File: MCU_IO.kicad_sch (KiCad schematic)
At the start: 31 parts, among them Q1 IRLML2803, SW1 SW_Omron_B3FS, SW2 SW_Omron_B3FS, U1 W25Q64JVSS, U2 RP2040, U3 MAX706RESA+, Y1 12MHz

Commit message: temp
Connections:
- net MCU_RX_Jetson is gone; now on net LoRa_CSn: U2.28 (GPIO17)
- net SD_CLK is gone; now on net LoRa_TX_EN: U2.34 (GPIO22)
- net SD_MISO is gone; now on net LoRa_RX_EN: U2.31 (GPIO20)
- net SD_MOSI is gone; now on net LoRa_BUSY: U2.35 (GPIO23)
- net 3V3_RST: no longer U2.9 (GPIO7)
- net Battery_ALERT: no longer U2.37 (GPIO25)
- net GPS_EN: no longer U2.8 (GPIO6)
- net I2C0_SCL: no longer U2.3 (GPIO1)
- net I2C0_SDA: no longer U2.2 (GPIO0)
- net I2C1_SCL: no longer U2.5 (GPIO3)
- net I2C1_SDA: no longer U2.4 (GPIO2)
- net IMU_INTn: no longer U2.29 (GPIO18)
- net IMU_RSTn: no longer U2.30 (GPIO19)
- net Jetson_EN: no longer U2.36 (GPIO24)
- net LoRa_BUSY: no longer U2.17 (GPIO14)
- net LoRa_CSn: no longer U2.12 (GPIO9)
- net LoRa_DIO1: now also U2.37 (GPIO25); no longer U2.38 (GPIO26_ADC0)
- net LoRa_DIO2: now also U2.36 (GPIO24); no longer U2.39 (GPIO27_ADC1)
- net LoRa_EN: no longer U2.15 (GPIO12)
- net LoRa_RSTn: now also U2.32 (GPIO21); no longer U2.16 (GPIO13)
- net LoRa_RX_EN: no longer U2.40 (GPIO28_ADC2)
- net LoRa_TX_EN: no longer U2.41 (GPIO29_ADC3)
- net SD_CSn: now also U2.38 (GPIO26_ADC0); no longer U2.32 (GPIO21)
- net WDT_WDI: no longer U2.18 (GPIO15)
- net LoRa_CLK: no longer names the net of U2.13 (GPIO10)
- net LoRa_MISO: no longer names the net of U2.11 (GPIO8)
- net LoRa_MOSI: no longer names the net of U2.14 (GPIO11)
- net MCU_RX_GPS: no longer names the net of U2.7 (GPIO5)
- net MCU_TX_GPS: no longer names the net of U2.6 (GPIO4)
- net MCU_TX_Jetson renamed SPI0_MISO
- new net SPI0_CLK: U2.29 (GPIO18)
- new net SPI0_MOSI: U2.30 (GPIO19)

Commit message: v1 done
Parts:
- removed C10: 2u2, Capacitor_SMD:C_0603_1608Metric, symbol Device:C_Small
- added C25: 2u2, Capacitor_SMD:C_0603_1608Metric, symbol Device:C_Small
- SW1, SW2: footprint Button_Switch_SMD:SW_SPST_Omron_B3FS-100xP -> Button_Switch_SMD:SW_SPST_Omron_B3FS-105xP
- U3: symbol MainBoard:MAX706RESA+ -> Argus-IC:MAX706RESA+
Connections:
- net +1V1: now also C25.1
- net 3V3_RST: now also U2.9 (GPIO7)
- net GND: now also C25.2
- net GPS_EN: now also U2.39 (GPIO27_ADC1)
- net I2C0_SCL: now also U2.3 (GPIO1)
- net I2C0_SDA: now also U2.2 (GPIO0)
- net I2C1_SCL: now also U2.5 (GPIO3)
- net I2C1_SDA: now also U2.4 (GPIO2)
- net IMU_INTn: now also U2.41 (GPIO29_ADC3)
- net Jetson_CSn: now also U2.12 (GPIO9)
- net LoRa_EN: now also U2.40 (GPIO28_ADC2)
- net SPI1_CLK: now also U2.13 (GPIO10)
- net SPI1_MISO: now also U2.11 (GPIO8)
- net SPI1_MOSI: now also U2.14 (GPIO11)
- net UART0_RX: now also U2.16 (GPIO13)
- net UART0_TX: now also U2.15 (GPIO12)
- net UART1_RX: now also U2.7 (GPIO5)
- net UART1_TX: now also U2.6 (GPIO4)
- net WDT_WDI: now also U2.8 (GPIO6)
- net RS485_TX_EN: now reaches U2.17 (GPIO14)
- net RS485_RX_EN: now reaches U2.18 (GPIO15)

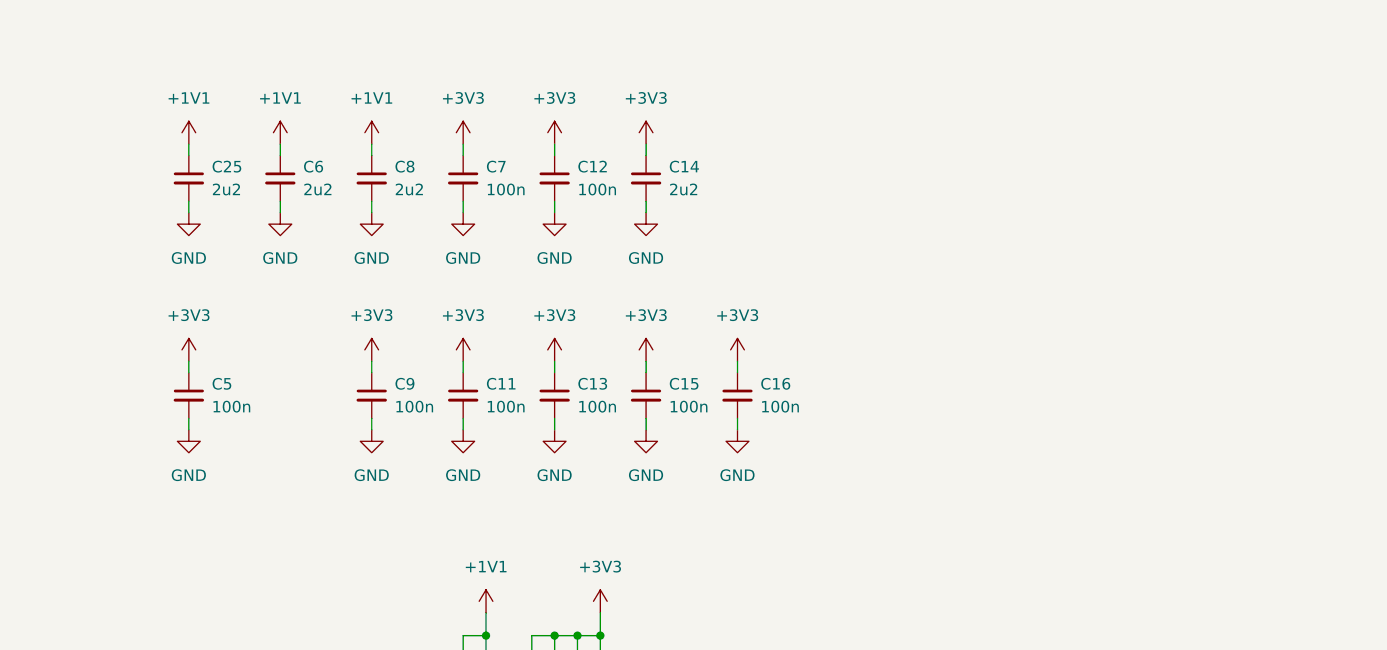
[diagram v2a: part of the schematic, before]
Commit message: Updated i2c device addresses and mcu caps
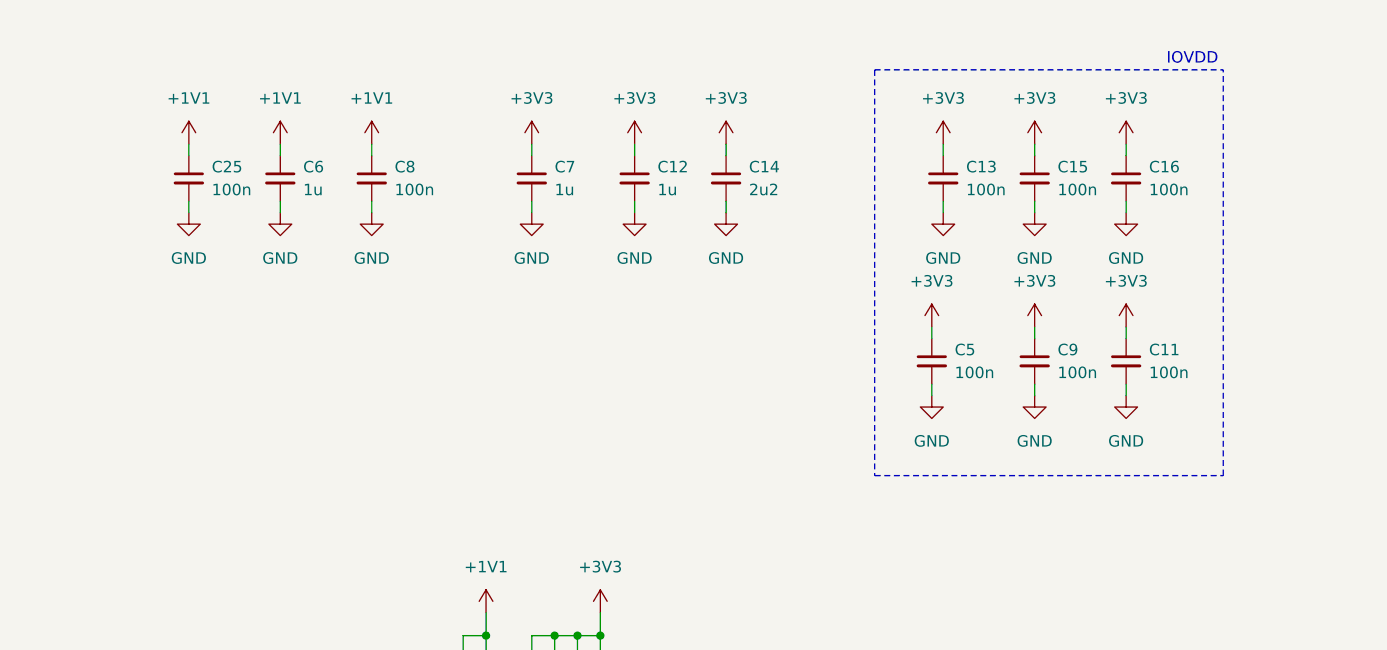
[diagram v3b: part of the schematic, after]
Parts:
- C12, C7: value 100n -> 1u
- C25, C8: value 2u2 -> 100n
- C6: value 2u2 -> 1u
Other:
- note added: "IOVDD"
- moved on the sheet: C11, C13, C15, C16, C5, C9

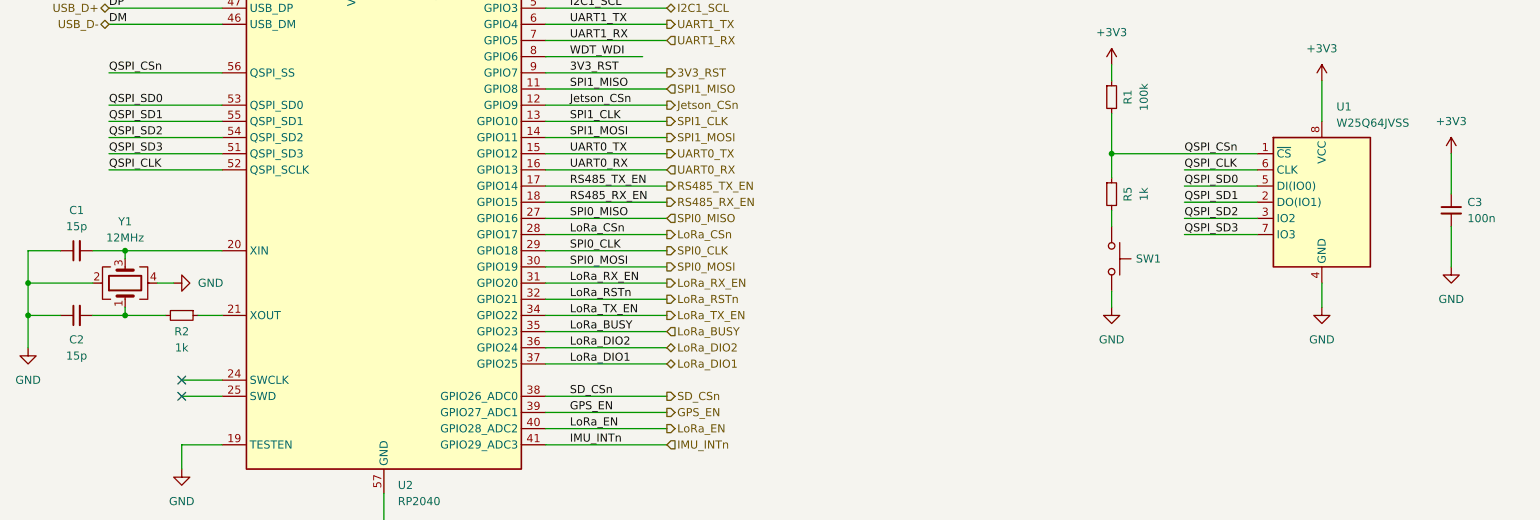
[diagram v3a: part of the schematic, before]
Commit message: Added extra connector
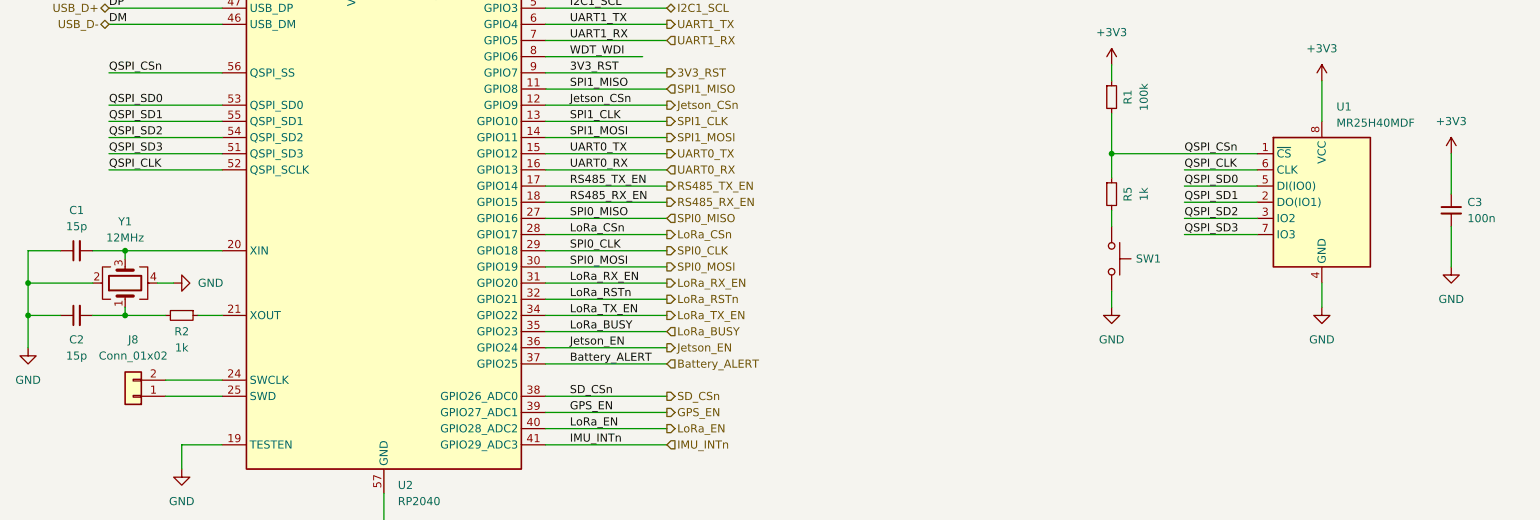
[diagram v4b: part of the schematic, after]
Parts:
- added J8: Conn_01x02, Connector_PinHeader_2.54mm:PinHeader_1x02_P2.54mm_Vertical, symbol Connector_Generic:Conn_01x02
- U1: value W25Q64JVSS -> MR25H40MDF; footprint Package_SO:SOIC-8_5.23x5.23mm_P1.27mm -> Package_DFN_QFN:DFN-8-1EP_6x5mm_P1.27mm_EP2x2mm
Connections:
- net at U2.24 (SWCLK): now also J8.2 (Pin_2)
- net at U2.25 (SWD): now also J8.1 (Pin_1)
- net LoRa_DIO1 renamed Battery_ALERT
- net LoRa_DIO2 renamed Jetson_EN
- no-connect marks 3 -> 1
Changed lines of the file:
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@@
 	)
 	(no_connect
-		(at 49.53 166.37)
-	)
-	(no_connect
 		(at 205.74 35.56)
 	)
-	(no_connect
-		(at 49.53 163.83)
-	)
 	(wire
 		(pts
@@
 	(wire
 		(pts
-			(xy 49.53 163.83) (xy 55.88 163.83)
-		)
-		(stroke
-			(width 0)
-			(type default)
-		)
-	)
-	(wire
-		(pts
 			(xy 195.58 149.86) (xy 195.58 152.4)
 		)
@@
 	(wire
 		(pts
+			(xy 46.99 163.83) (xy 55.88 163.83)
+		)
+		(stroke
+			(width 0)
+			(type default)
+		)
+	)
+	(wire
+		(pts
 			(xy 217.17 59.69) (xy 223.52 59.69)
 		)
@@
 	(wire
 		(pts
+			(xy 106.68 161.29) (xy 125.73 161.29)
+		)
+		(stroke
+			(width 0)
+			(type default)
+		)
+	)
+	(wire
+		(pts
 			(xy 106.68 120.65) (xy 125.73 120.65)
 		)
@@
 	(wire
 		(pts
-			(xy 106.68 158.75) (xy 125.73 158.75)
-		)
-		(stroke
-			(width 0)
-			(type default)
-		)
-	)
-	(wire
-		(pts
 			(xy 195.58 128.27) (xy 218.44 128.27)
 		)
@@
 	(wire
 		(pts
-			(xy 106.68 161.29) (xy 125.73 161.29)
-		)
-		(stroke
-			(width 0)
-			(type default)
-		)
-	)
-	(wire
-		(pts
 			(xy 223.52 72.39) (xy 219.71 72.39)
 		)
@@
 	(wire
 		(pts
+			(xy 46.99 166.37) (xy 55.88 166.37)
+		)
+		(stroke
+			(width 0)
+			(type default)
+		)
+	)
+	(wire
+		(pts
 			(xy 38.1 120.65) (xy 55.88 120.65)
 		)
@@
 	(wire
 		(pts
+			(xy 106.68 158.75) (xy 125.73 158.75)
+		)
+		(stroke
+			(width 0)
+			(type default)
+		)
+	)
+	(wire
+		(pts
 			(xy 193.04 38.1) (xy 193.04 40.64)
 		)
@@
 	(wire
 		(pts
-			(xy 49.53 166.37) (xy 55.88 166.37)
-		)
-		(stroke
-			(width 0)
-			(type default)
-		)
-	)
-	(wire
-		(pts
 			(xy 106.68 100.33) (xy 125.73 100.33)
 		)
@@
 		)
 	)
-	(label "LoRa_DIO2"
-		(at 110.49 158.75 0)
-		(fields_autoplaced yes)
-		(effects
-			(font
-				(size 1.27 1.27)
-			)
-			(justify left bottom)
-		)
-	)
 	(label "QSPI_SD3"
 		(at 38.1 128.27 0)
@@
 		)
 	)
+	(label "Battery_ALERT"
+		(at 110.49 161.29 0)
+		(fields_autoplaced yes)
+		(effects
+			(font
+				(size 1.27 1.27)
+			)
+			(justify left bottom)
+		)
+	)
 	(label "RESETn"
 		(at 194.31 72.39 0)
@@
 		)
 	)
-	(label "LoRa_DIO1"
-		(at 110.49 161.29 0)
+	(label "3V3_RST"
+		(at 110.49 115.57 0)
 		(fields_autoplaced yes)
 		(effects
@@
 		)
 	)
-	(label "3V3_RST"
-		(at 110.49 115.57 0)
+	(label "Jetson_EN"
+		(at 110.49 158.75 0)
 		(fields_autoplaced yes)
 		(effects
@@
 		)
 	)
-	(hierarchical_label "LoRa_DIO1"
-		(shape bidirectional)
-		(at 125.73 161.29 0)
-		(fields_autoplaced yes)
-		(effects
-			(font
-				(size 1.27 1.27)
-			)
-			(justify left)
-		)
-	)
 	(hierarchical_label "RS485_RX_EN"
 		(shape output)
@@
 		)
 	)
-	(hierarchical_label "I2C0_SDA"
-		(shape bidirectional)
-		(at 125.73 97.79 0)
+	(hierarchical_label "Battery_ALERT"
+		(shape input)
+		(at 125.73 161.29 0)
 		(fields_autoplaced yes)
 		(effects
@@
 		)
 	)
-	(hierarchical_label "LoRa_DIO2"
+	(hierarchical_label "I2C0_SDA"
 		(shape bidirectional)
-		(at 125.73 158.75 0)
+		(at 125.73 97.79 0)
 		(fields_autoplaced yes)
 		(effects
@@
 		)
 	)
+	(hierarchical_label "Jetson_EN"
+		(shape output)
+		(at 125.73 158.75 0)
+		(fields_autoplaced yes)
+		(effects
+			(font
+				(size 1.27 1.27)
+			)
+			(justify left)
+		)
+	)
 	(hierarchical_label "SPI1_MISO"
 		(shape input)
@@
 	)
 	(symbol
+		(lib_id "Connector_Generic:Conn_01x02")
+		(at 41.91 166.37 180)
+		(unit 1)
+		(exclude_from_sim no)
+		(in_bom yes)
+		(on_board yes)
+		(dnp no)
+		(fields_autoplaced yes)
+		(property "Reference" "J8"
+			(at 41.91 157.48 0)
+			(effects
+				(font
+					(size 1.27 1.27)
+				)
+			)
+		)
+		(property "Value" "Conn_01x02"
+			(at 41.91 160.02 0)
+			(effects
+				(font
+					(size 1.27 1.27)
+				)
+			)
+		)
+		(property "Footprint" "Connector_PinHeader_2.54mm:PinHeader_1x02_P2.54mm_Vertical"
+			(at 41.91 166.37 0)
+			(effects
+				(font
+					(size 1.27 1.27)
+				)
+				(hide yes)
+			)
+		)
+		(property "Datasheet" "~"
+			(at 41.91 166.37 0)
+			(effects
+				(font
+					(size 1.27 1.27)
+				)
+				(hide yes)
+			)
+		)
+		(property "Description" "Generic connector, single row, 01x02, script generated (kicad-library-utils/schlib/autogen/connector/)"
+			(at 41.91 166.37 0)
+			(effects
+				(font
+					(size 1.27 1.27)
+				)
+				(hide yes)
+			)
+		)
+		(pin "2"
+		)
+		(pin "1"
+		)
+		(instances
+			(project ""
+				(path "/4c932743-8c6f-426e-9c1f-5a3f2b32c70d/21e71e76-dfb6-4af2-84cc-797c0fdddabe"
+					(reference "J8")
+					(unit 1)
+				)
+			)
+		)
+	)
+	(symbol
 		(lib_id "Device:R_Small")
 		(at 195.58 134.62 0)
@@
 			)
 		)
-		(property "Value" "W25Q64JVSS"
+		(property "Value" "MR25H40MDF"
 			(at 230.886 123.444 0)
 			(effects
@@
 			)
 		)
-		(property "Footprint" "Package_SO:SOIC-8_5.23x5.23mm_P1.27mm"
+		(property "Footprint" "Package_DFN_QFN:DFN-8-1EP_6x5mm_P1.27mm_EP2x2mm"
 			(at 228.6 135.89 0)
 			(effects

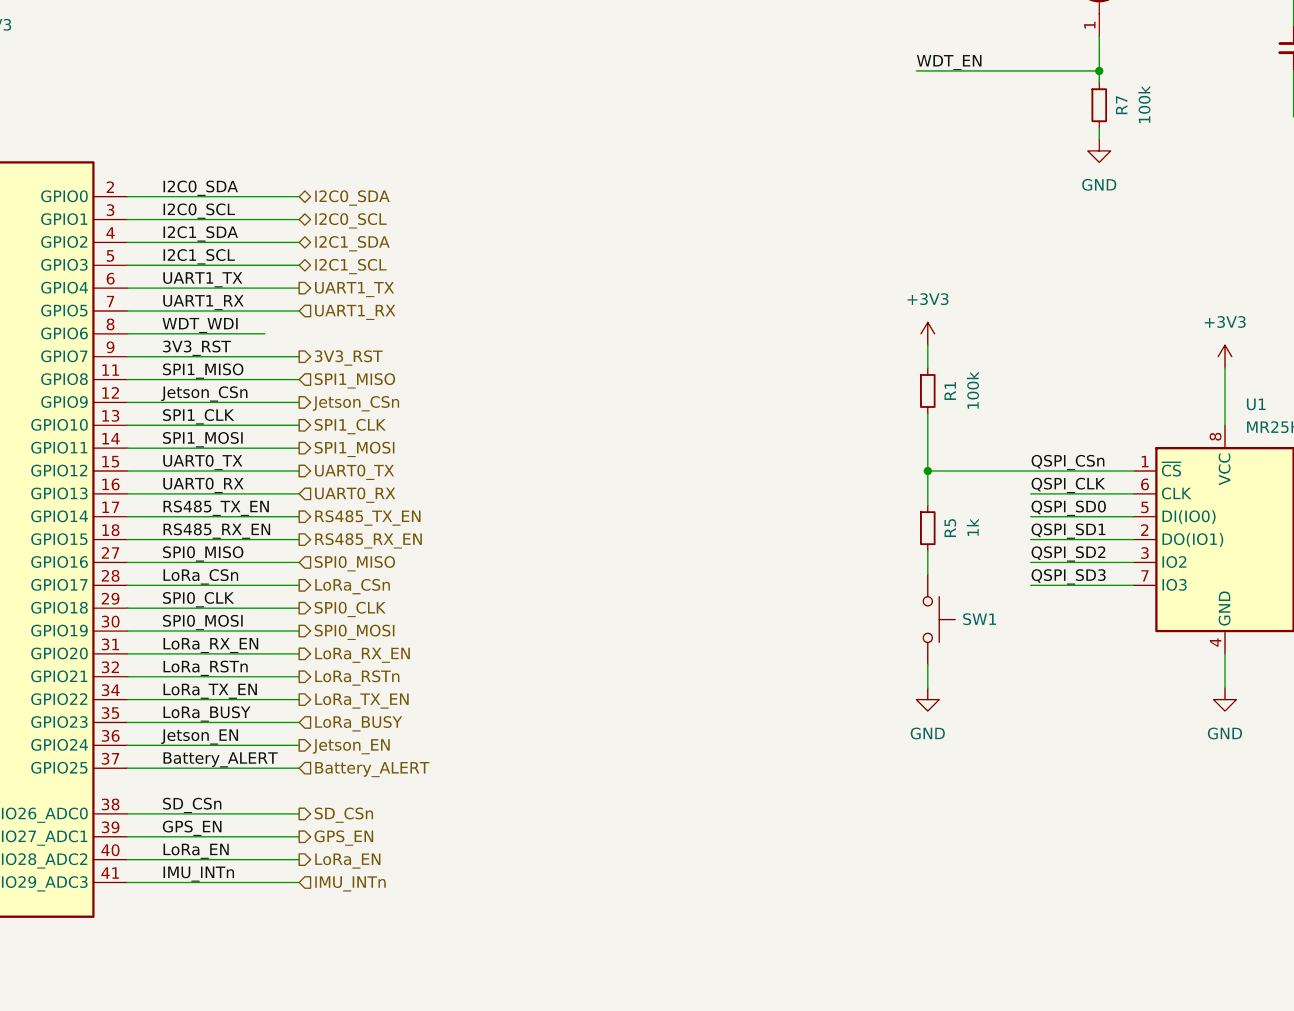
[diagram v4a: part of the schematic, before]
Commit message: Added better protection to SD card, Jetson IO, and added address breakouts to power monitors
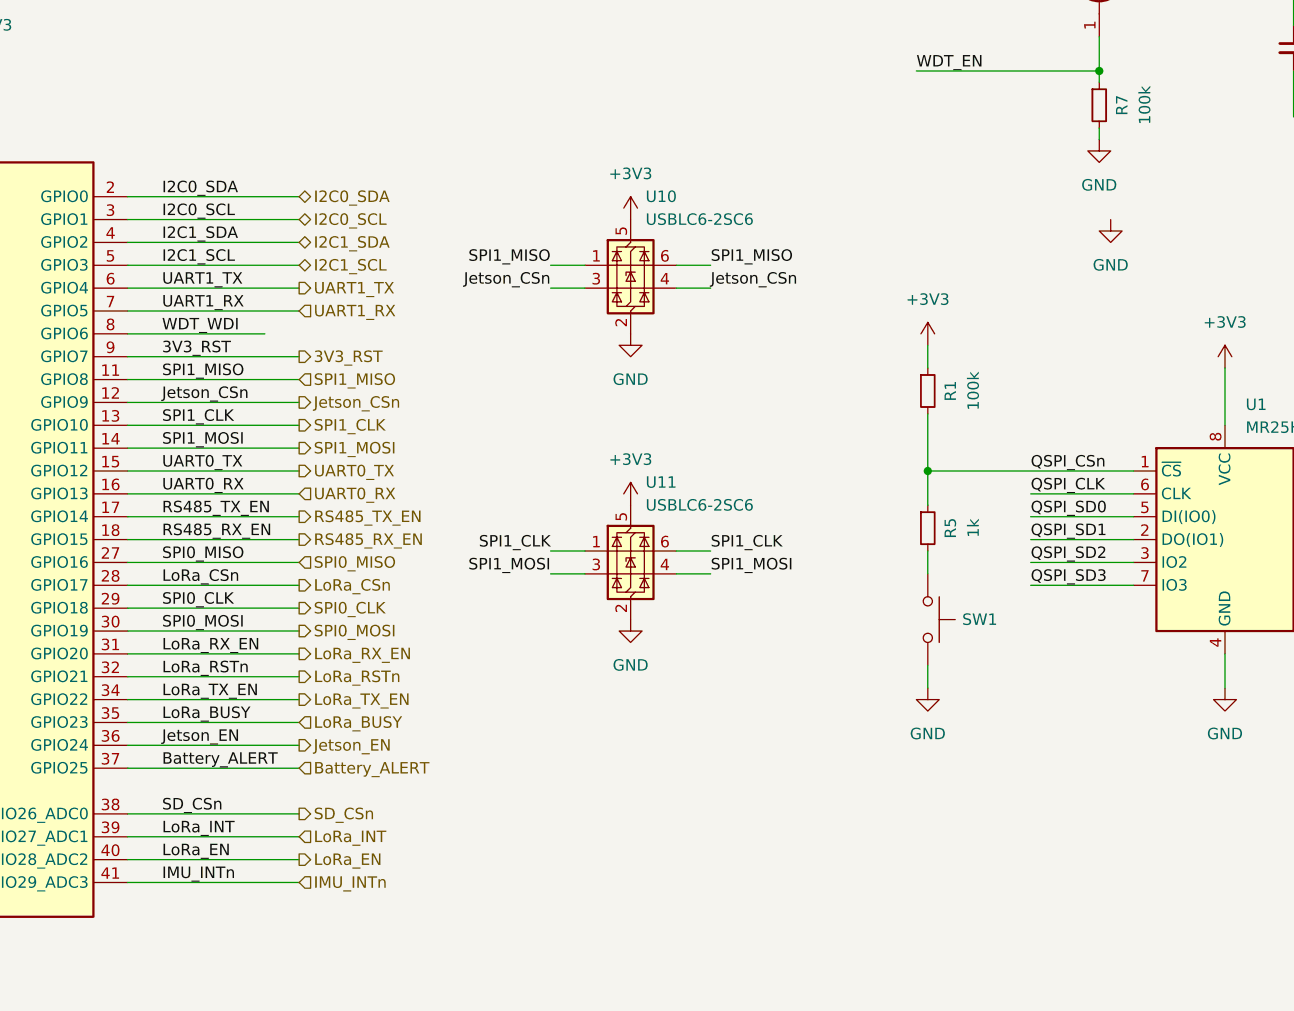
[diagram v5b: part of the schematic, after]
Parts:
- added U10, U11: USBLC6-2SC6, Package_TO_SOT_SMD:SOT-23-6, symbol Power_Protection:USBLC6-2SC6
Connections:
- net +3V3: now also U10.5 (VBUS), U11.5 (VBUS)
- net GND: now also U10.2 (GND), U11.2 (GND)
- net Jetson_CSn: now also U10.3 (I/O2), U10.4 (I/O2)
- net SPI1_CLK: now also U11.1 (I/O1), U11.6 (I/O1)
- net SPI1_MISO: now also U10.1 (I/O1), U10.6 (I/O1)
- net SPI1_MOSI: now also U11.3 (I/O2), U11.4 (I/O2)
- net GPS_EN renamed LoRa_INT

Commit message: Updated version to v2.1
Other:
- company: (none) -> Carnegie Mellon University
- title: (none) -> Argus Mainboard
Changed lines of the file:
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@@
 	(generator_version "8.0")
 	(paper "A4")
+	(title_block
+		(title "Argus Mainboard")
+		(date "2024-11-19")
+		(rev "v2.1")
+		(company "Carnegie Mellon University")
+		(comment 1 "M. Holliday")
+		(comment 2 "N. Khera")
+		(comment 3 "V. Rajesh")
+	)
 	(junction
 		(at 195.58 128.27)
